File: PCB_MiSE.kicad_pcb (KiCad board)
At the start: 2 copper layers, 75 x 80.2 mm, 40 parts, among them IC1 MSP430FR2355TPT, J1 WIFI, J10 Conn_01x01, J11 Conn_01x01, J2 Conn_01x03, J3 Conn_01x01, J4 Clk read conn, J5 Conn_01x01, J6 Display, J7 Conn_01x01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

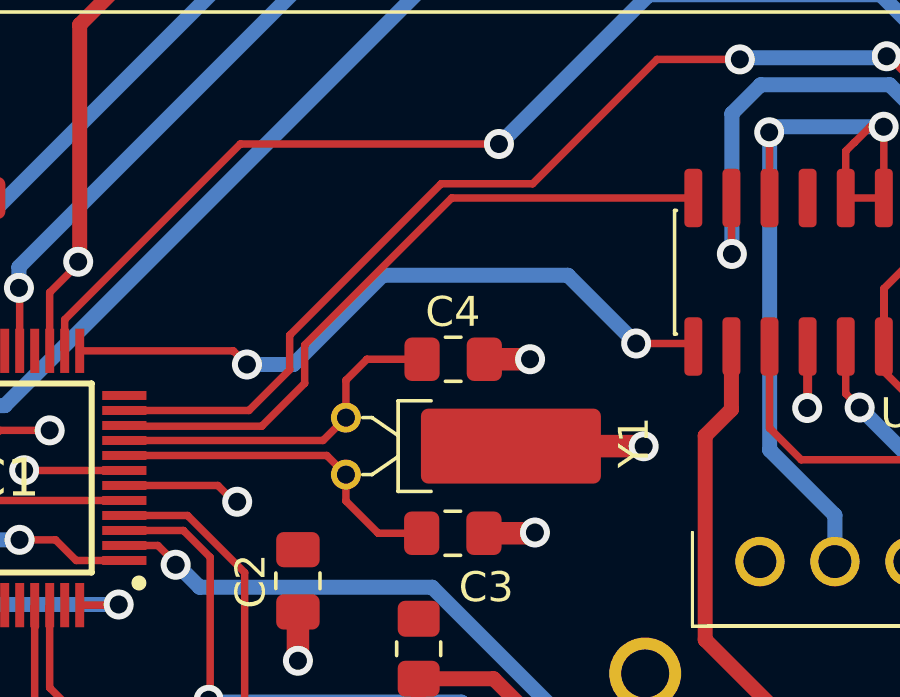
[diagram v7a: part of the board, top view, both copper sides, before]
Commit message: falta cambiar pulsadores
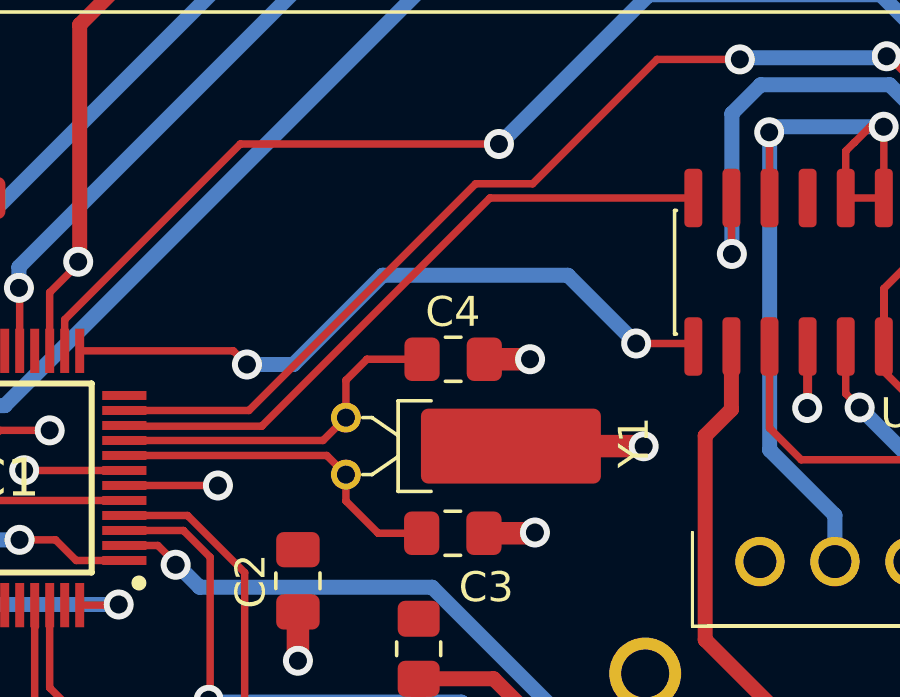
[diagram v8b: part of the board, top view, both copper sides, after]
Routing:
- net VCC: track 3.89 -> 3.12 mm
- net GPIOl: track 22.9 -> 22.1 mm
- net GPIOr: track 36.4 -> 35.7 mm
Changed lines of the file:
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@@
 		(net 2)
 	)
-	(segment
-		(start 74.75 92.35)
-		(end 74.208 91.808)
-		(width 0.25)
-		(layer "F.Cu")
-		(net 2)
-	)
-	(via
-		(at 74.85 92.35)
+	(via
+		(at 74.208 91.808)
 		(size 1)
 		(drill 0.6)
@@
 	)
 	(segment
-		(start 76.6 87.95)
-		(end 76.6 86.8)
+		(start 75.242 89.308)
+		(end 82.8 81.75)
+		(width 0.25)
+		(layer "F.Cu")
+		(net 34)
+	)
+	(segment
+		(start 96.5 77.5)
+		(end 96.415 77.585)
+		(width 0.25)
+		(layer "F.Cu")
+		(net 34)
+	)
+	(segment
+		(start 82.8 81.75)
+		(end 84.7 81.75)
+		(width 0.25)
+		(layer "F.Cu")
+		(net 34)
+	)
+	(segment
+		(start 96.415 77.585)
+		(end 96.635 77.585)
+		(width 0.25)
+		(layer "F.Cu")
+		(net 34)
+	)
+	(segment
+		(start 84.7 81.75)
+		(end 88.845 77.605)
+		(width 0.25)
+		(layer "F.Cu")
+		(net 34)
+	)
+	(segment
+		(start 96.635 77.585)
+		(end 97.675 78.625)
 		(width 0.25)
 		(layer "F.Cu")
@@
 		(net 34)
 	)
-	(segment
-		(start 81.65 81.75)
-		(end 84.7 81.75)
-		(width 0.25)
-		(layer "F.Cu")
-		(net 34)
-	)
-	(segment
-		(start 96.5 77.5)
-		(end 96.415 77.585)
-		(width 0.25)
-		(layer "F.Cu")
-		(net 34)
-	)
-	(segment
-		(start 84.7 81.75)
-		(end 88.845 77.605)
-		(width 0.25)
-		(layer "F.Cu")
-		(net 34)
-	)
-	(segment
-		(start 76.6 86.8)
-		(end 81.65 81.75)
-		(width 0.25)
-		(layer "F.Cu")
-		(net 34)
-	)
-	(segment
-		(start 96.415 77.585)
-		(end 96.635 77.585)
-		(width 0.25)
-		(layer "F.Cu")
-		(net 34)
-	)
-	(segment
-		(start 75.242 89.308)
-		(end 76.6 87.95)
-		(width 0.25)
-		(layer "F.Cu")
-		(net 34)
-	)
-	(segment
-		(start 96.635 77.585)
-		(end 97.675 78.625)
-		(width 0.25)
-		(layer "F.Cu")
-		(net 34)
-	)
 	(via
 		(at 91.605 77.605)
@@
 	)
 	(segment
-		(start 77.1 88.4)
-		(end 75.668 89.832)
-		(width 0.25)
-		(layer "F.Cu")
-		(net 35)
-	)
-	(segment
-		(start 77.1 87.125)
-		(end 77.1 88.4)
-		(width 0.25)
-		(layer "F.Cu")
-		(net 35)
-	)
-	(segment
 		(start 75.668 89.832)
 		(end 71.112 89.832)
@@
 	)
 	(segment
+		(start 90.055 82.225)
+		(end 83.275 82.225)
+		(width 0.25)
+		(layer "F.Cu")
+		(net 35)
+	)
+	(segment
+		(start 83.275 82.225)
+		(end 75.668 89.832)
+		(width 0.25)
+		(layer "F.Cu")
+		(net 35)
+	)
+	(segment
 		(start 71.112 89.832)
 		(end 71.088 89.808)
 		(width 0.25)
 		(layer "F.Cu")
-		(net 35)
-	)
-	(segment
-		(start 82 82.225)
-		(end 77.1 87.125)
-		(width 0.25)
-		(layer "F.Cu")
-		(net 35)
-	)
-	(segment
-		(start 90.055 82.225)
-		(end 82 82.225)
-		(width 0.25)
-		(layer "F.Cu")
